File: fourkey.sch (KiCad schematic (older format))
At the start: 6 parts, among them K1 KEYSW, K2 KEYSW, K3 KEYSW, K4 KEYSW, SW1 SW_PUSH, U1 ProMicro

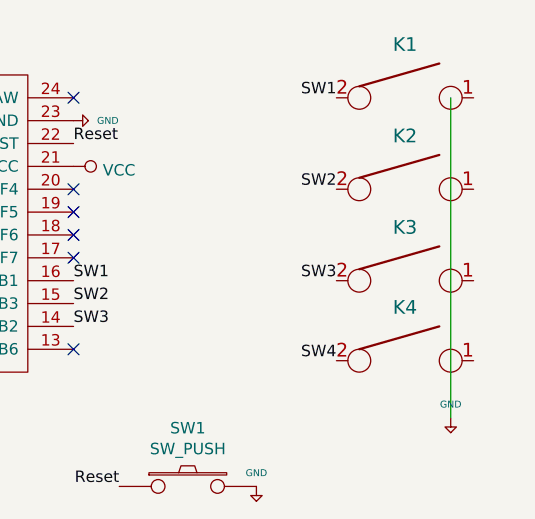
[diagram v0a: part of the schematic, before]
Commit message: flip pro micro. remove one set of mousebites
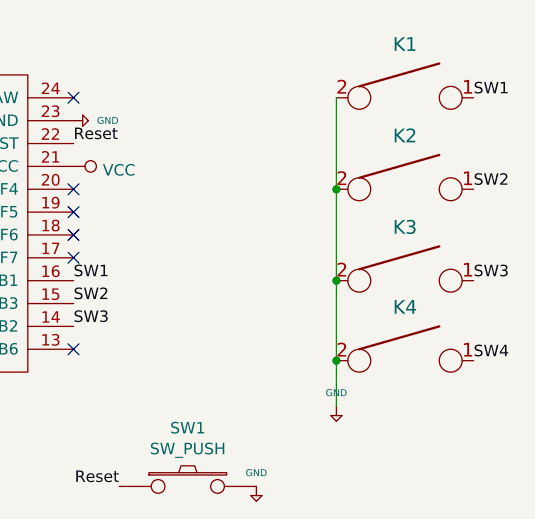
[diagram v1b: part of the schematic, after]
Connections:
- wire segments 1 -> 4
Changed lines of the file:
@@
 L keyboard_parts:GND #PWR0101
 U 1 1 6035B7A5
-P 5900 3400
-F 0 "#PWR0101" H 5900 3450 20  0001 C CNN
-F 1 "GND" H 5900 3459 30  0000 C CNN
-F 2 "" H 5900 3400 60  0000 C CNN
-F 3 "" H 5900 3400 60  0000 C CNN
-	1    5900 3400
+P 5400 3350
+F 0 "#PWR0101" H 5400 3400 20  0001 C CNN
+F 1 "GND" H 5400 3409 30  0000 C CNN
+F 2 "" H 5400 3350 60  0000 C CNN
+F 3 "" H 5400 3350 60  0000 C CNN
+	1    5400 3350
 	1    0    0    -1
 $EndComp
-Wire Wire Line
-	5900 2000 5900 3400
 Text Label 4250 3000 0    50   ~ 0
 SW3
@@
 	1    0    0    -1
 $EndComp
-Text Label 5400 2000 2    50   ~ 0
-SW1
-Text Label 5400 2400 2    50   ~ 0
+Text Label 6000 2400 0    50   ~ 0
 SW2
-Text Label 5400 2800 2    50   ~ 0
+Text Label 6000 2800 0    50   ~ 0
 SW3
-Text Label 5400 3150 2    50   ~ 0
+Text Label 6000 3150 0    50   ~ 0
 SW4
 Text Label 4450 3700 2    50   ~ 0
@@
 SW4
 NoConn ~ 2850 2900
+Text Label 6000 2000 0    50   ~ 0
+SW1
+Wire Wire Line
+	5400 2000 5400 2400
+Connection ~ 5400 2400
+Wire Wire Line
+	5400 2400 5400 2800
+Connection ~ 5400 2800
+Wire Wire Line
+	5400 2800 5400 3150
+Connection ~ 5400 3150
+Wire Wire Line
+	5400 3150 5400 3350
 $EndSCHEMATC
